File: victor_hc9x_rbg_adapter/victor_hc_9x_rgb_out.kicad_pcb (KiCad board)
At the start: 2 copper layers, 99.5 x 69 mm, 24 parts, among them J1 DB25_Female_MountingHoles, J2 SCART-F, J3 RIGHT, J4 DIN-8, J5 VIDEO, J6 LEFT, U1 ICL7660

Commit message: Add files via upload
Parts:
- moved J4 2.43 mm to (135.8, 107.3)
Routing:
- net ASPECT_RATIO: track 133.4 -> 93.6 mm
- net B: track 59.2 -> 37.1 mm, vias 2 -> 1
- net GND: track 245.4 -> 258.3 mm
- net C_VIDEO_IN: track 54.5 -> 43.0 mm, vias 1 -> 0
- net B_2: track 35.7 -> 24.7 mm
- net SHIELD: track 90.8 -> 101.4 mm
- net L_AUDIO_OUT: track 87.3 -> 96.5 mm
- net C_VIDEO_OUT: track 77.4 -> 69.3 mm, vias 0 -> 1
- net G_2: track 26.5 -> 32.8 mm
- net R_AUDIO_OUT: track 61.5 -> 56.1 mm, vias 1 -> 0
- net R_AUDIO_IN_2: track 31.3 -> 27.3 mm, vias 0 -> 1
- net L_AUDIO_IN_2: track 17.0 -> 13.4 mm
- net R_AUDIO_IN: track 65.9 -> 62.8 mm
- net RGB_switching: track 67.4 -> 64.9 mm
- net R_2: track 7.74 -> 5.31 mm
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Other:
- board size 99.5 x 69 mm -> 99.5 x 68.6 mm
- board text added: "A/V IN"
- board text added: "DIN8 RGB-OUT"
- board text added: "SCART-OUTPUT"

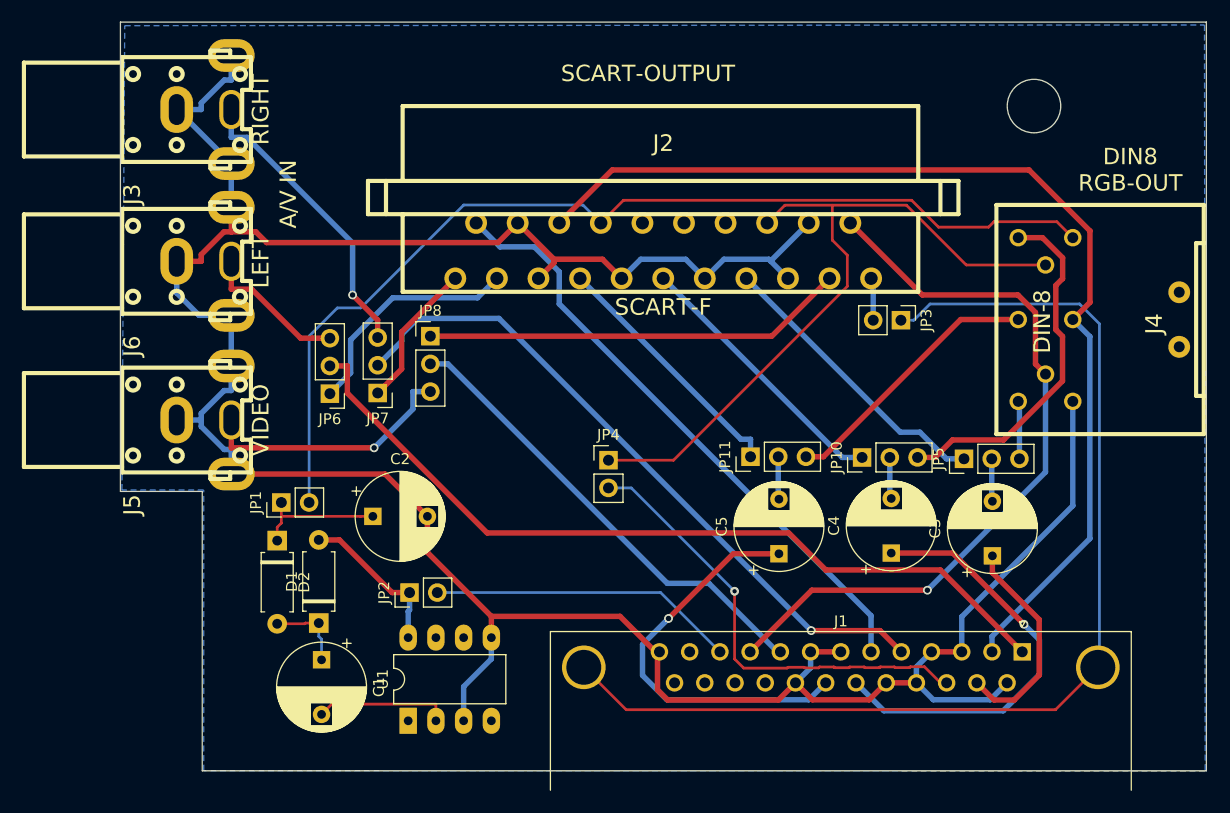
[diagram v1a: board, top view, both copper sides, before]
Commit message: fixed din-8 footprint and scart connections
din-8 was mirrored, so now corrected. scart pins were not correct related to in and out audio/video. only rca audio/video input was correct towards db25 connector.
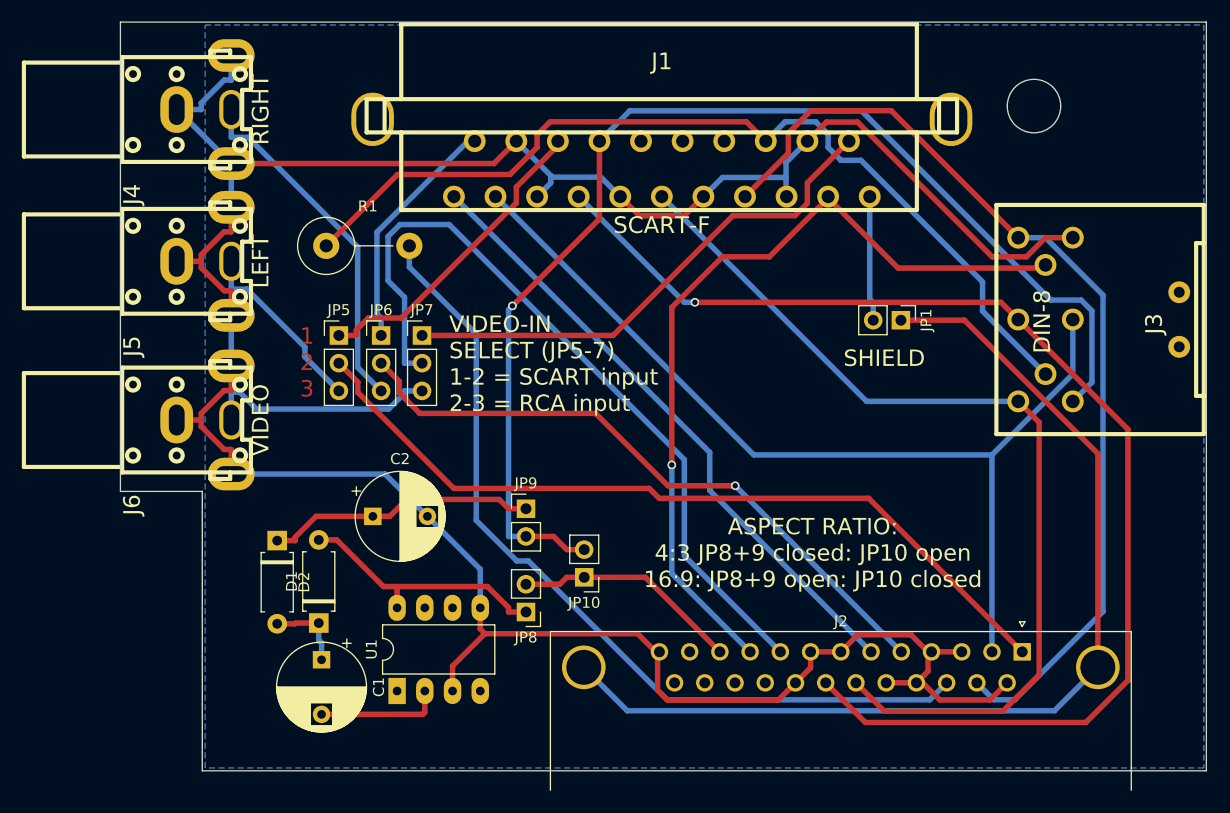
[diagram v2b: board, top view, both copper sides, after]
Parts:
- removed C3, C4, C5: 100uF/16v, Capacitor_THT:CP_Radial_D8.0mm_P5.00mm
- removed JP11: B_1_x_2, Connector_PinHeader_2.54mm:PinHeader_1x03_P2.54mm_Vertical
- removed JP4: RGB_SW, Connector_PinHeader_2.54mm:PinHeader_1x02_P2.54mm_Vertical
- removed the JP5 at (125.8, 120.0)
- added R1: 100R, Resistor_THT:R_Axial_DIN0516_L15.5mm_D5.0mm_P7.62mm_Vertical, F.Cu at (67.4, 100.5)
- JP10: value G_1_x_2 -> 16:9; footprint Connector_PinHeader_2.54mm:PinHeader_1x03_P2.54mm_Vertical -> Connector_PinHeader_2.54mm:PinHeader_1x02_P2.54mm_Vertical
- JP8: renamed from JP2; value AVCTRL -> 4:3
- JP9: renamed from JP1; value ASPECTR -> 4:3
- moved JP10 27.7 mm to (91.0, 130.9), turned to 180 degrees
- moved JP9 22.4 mm to (85.7, 124.6), turned to 0 degrees
- moved JP8 10.8 mm to (85.7, 134.0), turned to 180 degrees
- moved J1 7.49 mm to (98.1, 88.7)
- moved JP5 5.40 mm to (68.5, 108.7), turned to 0 degrees
- moved JP6 5.28 mm to (72.4, 108.7), turned to 0 degrees
- moved U1 2.91 mm to (73.9, 141.3)
- moved JP7 0.76 mm to (76.1, 108.7)
- renumbered J2 to J1, J1 to J2, J4 to J3, J3 to J4, J6 to J5, J5 to J6, JP3 to JP1, JP6 to JP5, JP7 to JP6, JP8 to JP7
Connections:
- J1 pad 1: R_AUDIO_IN_1 -> R_AUDIO_OUT
- J1 pad 11: G_1 -> G
- J1 pad 15: R_1 -> R
- J1 pad 19: C_VIDEO_IN_1 -> C_VIDEO_OUT
- J1 pad 2: R_AUDIO_OUT -> R_AUDIO_IN_1
- J1 pad 20: C_VIDEO_OUT -> C_VIDEO_IN_1
- J1 pad 3: L_AUDIO_IN_1 -> L_AUDIO_OUT
- J1 pad 6: L_AUDIO_OUT -> L_AUDIO_IN_1
- J1 pad 7: B_1 -> B
- J3 pad 6: R_2 -> R
- J3 pad 7: G_2 -> G
- J3 pad 8: B_2 -> B
- JP10 pad 1: G_1 -> AV_CTRL
- JP10 pad 2: Net-(C4-Pad2) -> ASPECT_RATIO
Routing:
- net B: track 37.1 -> 113.0 mm
- net R: track 20.0 -> 88.7 mm
- net G: track 39.3 -> 85.5 mm, vias 1 -> 0
- net Ys: track 42.3 -> 78.2 mm, vias 1 -> 0
- net G_2: track 32.8 -> 0.00 mm
- net C_VIDEO_IN: track 43.0 -> 71.6 mm
- net R_1: track 26.8 -> 0.00 mm
- net G_1: track 25.0 -> 0.00 mm
- net B_2: track 24.7 -> 0.00 mm
- net B_1: track 23.3 -> 0.00 mm
- net RGB_switching: track 64.9 -> 84.6 mm
- net ASPECT_RATIO: track 93.6 -> 110.0 mm, vias 0 -> 1
- net Net-(C2-Pad1): track 12.0 -> 24.9 mm
- net Net-(D1-Pad2): track 14.5 -> 23.9 mm
- net C_VIDEO_IN_1: track 38.8 -> 47.6 mm
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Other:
- board text added: "1 2 3"
- board text added: "ASPECT RATIO: 4:3 JP8+9 closed: JP10 open 16:9: JP8+9 open: JP10 closed"
- board text added: "SHIELD"
- board text added: "VIDEO-IN SELECT (JP5-7) 1-2 = SCART input 2-3 = RCA input"
- board text removed: "A/V IN"
- board text removed: "DIN8 RGB-OUT"
- board text removed: "SCART-OUTPUT"
